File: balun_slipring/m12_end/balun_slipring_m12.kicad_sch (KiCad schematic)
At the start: 7 parts, among them J1 M12 A-8 FEMALE / EXACT MPN TBD, J2 SMA_A, J3 SMA_B, T1 ADT2-1T+, T2 ADT2-1T+

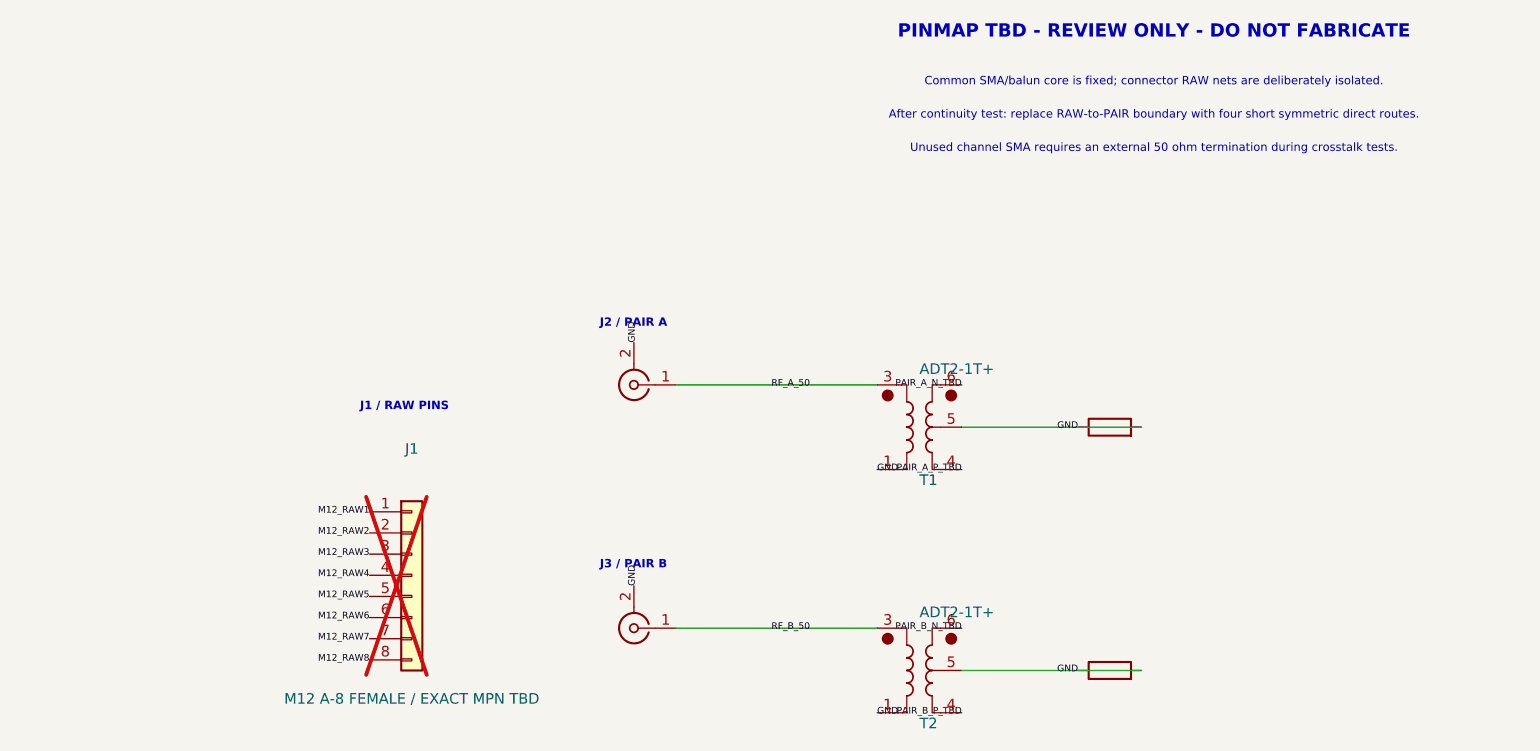
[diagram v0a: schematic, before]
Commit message: feat: finalize slip-ring fixtures and floating CT baseline
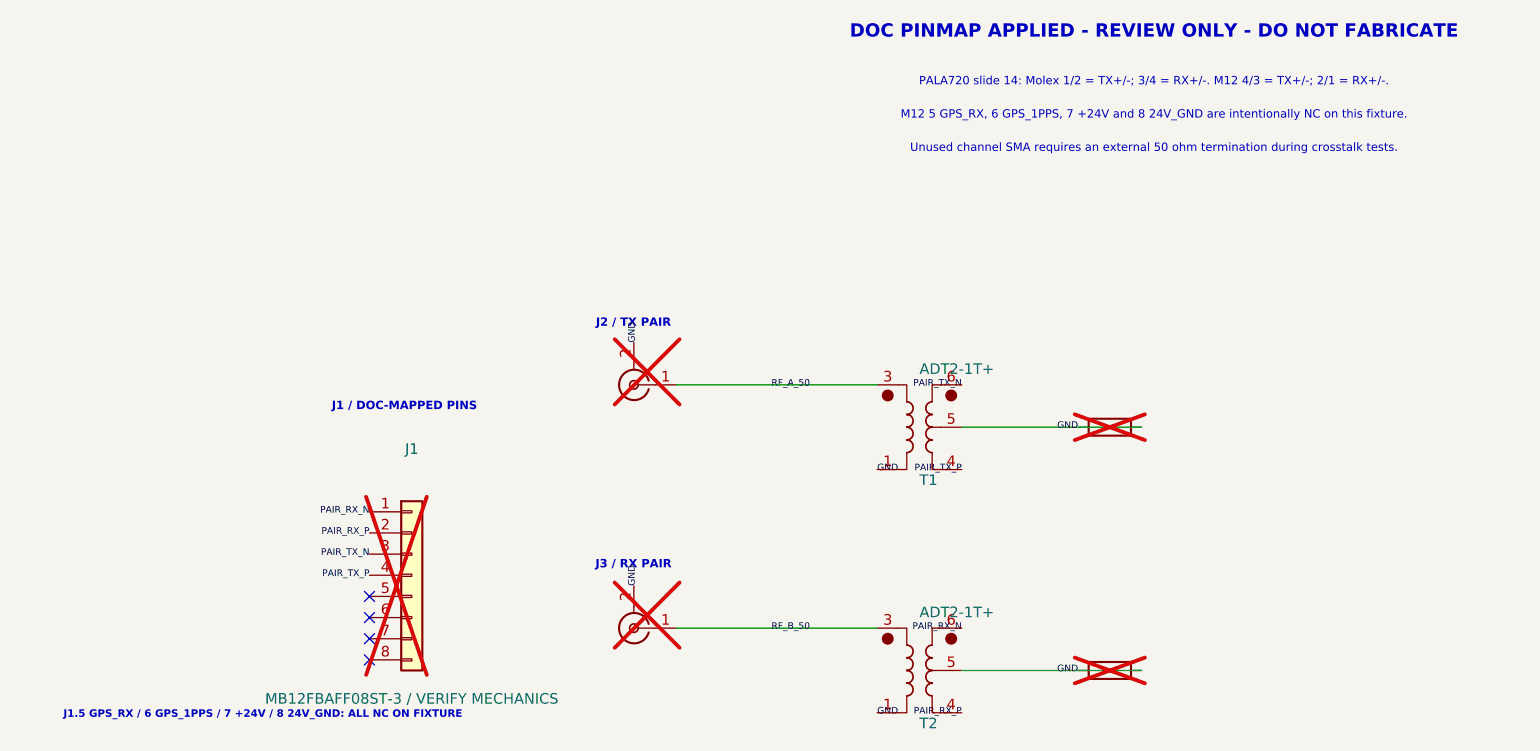
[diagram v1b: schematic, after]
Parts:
- J1: value M12 A-8 FEMALE / EXACT MPN TBD -> MB12FBAFF08ST-3 / VERIFY MECHANICS; footprint (none) -> balun_slipring_common:Finecables_MB12FBAFF08ST-3; Assembly TBD / DO NOT ORDER OR FABRICATE -> BACK-SIDE CANDIDATE; DNP UNTIL MATING, KEY/PIN-1 ORIENTATIO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; MPN Female mate for MB12MBAFF08ST-0; suffix TBD -> MB12FBAFF08ST-3 (candidate; verify mechanics); Manufacturer Finecables (candidate family) -> Finecables
- J2, J3: now not fitted
- RCT1, RCT2: Assembly FIT; remove for floating-CT comparison -> DNP; fit all four RCTs only for controlled CT-GND comparison; now not fitted
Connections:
- net PAIR_A_N_TBD is gone; now on net PAIR_TX_N: T1.6
- net PAIR_A_P_TBD is gone; now on net PAIR_TX_P: T1.4
- net PAIR_B_N_TBD is gone; now on net PAIR_RX_N: T2.6
- net PAIR_B_P_TBD is gone; now on net PAIR_RX_P: T2.4
- net M12_RAW1 renamed PAIR_RX_N
- net M12_RAW2 renamed PAIR_RX_P
- net M12_RAW3 renamed PAIR_TX_N
- net M12_RAW4 renamed PAIR_TX_P
- net M12_RAW5: no longer names the net of J1.5 (Pin_5)
- net M12_RAW6: no longer names the net of J1.6 (Pin_6)
- net M12_RAW7: no longer names the net of J1.7 (Pin_7)
- net M12_RAW8: no longer names the net of J1.8 (Pin_8)
- no-connect marks 0 -> 4
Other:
- note added: "DOC PINMAP APPLIED - REVIEW ONLY - DO NOT FABRICATE"
- note added: "J1 / DOC-MAPPED PINS"
- note added: "J1.5 GPS_RX / 6 GPS_1PPS / 7 +24V / 8 24V_GND: ALL NC ON FIXTURE"
- note added: "J2 / TX PAIR"
- note added: "J3 / RX PAIR"
- note added: "M12 5 GPS_RX, 6 GPS_1PPS, 7 +24V and 8 24V_GND are intentionally NC on this fixture."
- note added: "PALA720 slide 14: Molex 1/2 = TX+/-; 3/4 = RX+/-. M12 4/3 = TX+/-; 2/1 = RX+/-."
- note removed: "After continuity test: replace RAW-to-PAIR boundary with four short symmetric direct routes."
- note removed: "Common SMA/balun core is fixed; connector RAW nets are deliberately isolated."
- note removed: "J1 / RAW PINS"
- note removed: "J2 / PAIR A"
- note removed: "J3 / PAIR B"
- note removed: "PINMAP TBD - REVIEW ONLY - DO NOT FABRICATE"
- title: 100BASE-TX slip-ring VNA fixture - M12 END - PINMAP TBD -> 100BASE-TX slip-ring VNA fixture - M12 END - DOC PINMAP
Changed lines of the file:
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@@
 	(paper "A4")
 	(title_block
-		(title "100BASE-TX slip-ring VNA fixture - M12 END - PINMAP TBD")
+		(title "100BASE-TX slip-ring VNA fixture - M12 END - DOC PINMAP")
 		(date "2026-08-13")
-		(rev "DRAFT 0")
+		(rev "DRAFT 1")
 		(comment 1 "Two-channel 50 ohm single-ended to 100 ohm differential fixture core.")
-		(comment 2 "Connector RAW pins intentionally not mapped to balun pairs.")
-		(comment 3 "REVIEW ONLY - DO NOT FABRICATE UNTIL PINMAP AND CONNECTOR MECHANICS ARE VERIFIED.")
-	)
-	(text "PINMAP TBD - REVIEW ONLY - DO NOT FABRICATE"
+		(comment 2 "Electrical map from PALA720 slide 14; TX and RX fan-outs are connected.")
+		(comment 3 "REVIEW ONLY - DO NOT FABRICATE UNTIL CONTINUITY, CONNECTOR MECHANICS AND SMA STACK ARE VERIFIED.")
+	)
+	(text "DOC PINMAP APPLIED - REVIEW ONLY - DO NOT FABRICATE"
 		(exclude_from_sim no)
 		(at 145 25 0)
@@
 		)
 	)
-	(text "Common SMA/balun core is fixed; connector RAW nets are deliberately isolated."
+	(text "PALA720 slide 14: Molex 1/2 = TX+/-; 3/4 = RX+/-. M12 4/3 = TX+/-; 2/1 = RX+/-."
 		(exclude_from_sim no)
 		(at 145 31 0)
@@
 		)
 	)
-	(text "After continuity test: replace RAW-to-PAIR boundary with four short symmetric direct routes."
+	(text "M12 5 GPS_RX, 6 GPS_1PPS, 7 +24V and 8 24V_GND are intentionally NC on this fixture."
 		(exclude_from_sim no)
 		(at 145 35 0)
@@
 		)
 	)
-	(text "J2 / PAIR A"
+	(text "J2 / TX PAIR"
 		(exclude_from_sim no)
 		(at 82.5 60 0)
@@
 		)
 	)
-	(text "J3 / PAIR B"
+	(text "J3 / RX PAIR"
 		(exclude_from_sim no)
 		(at 82.5 89 0)
@@
 		)
 	)
-	(text "J1 / RAW PINS"
+	(text "J1 / DOC-MAPPED PINS"
 		(exclude_from_sim no)
 		(at 55 70 0)
@@
 		)
 	)
-	(label "PAIR_A_N_TBD"
+	(label "PAIR_TX_N"
 		(at 121.92 67.31 180)
 		(effects
@@
 		)
 	)
-	(label "PAIR_A_P_TBD"
+	(label "PAIR_TX_P"
 		(at 121.92 77.47 180)
 		(effects
@@
 		)
 	)
-	(label "PAIR_B_N_TBD"
+	(label "PAIR_RX_N"
 		(at 121.92 96.52 180)
 		(effects
@@
 		)
 	)
-	(label "PAIR_B_P_TBD"
+	(label "PAIR_RX_P"
 		(at 121.92 106.68 180)
 		(effects
@@
 		)
 	)
-	(label "M12_RAW1"
+	(label "PAIR_RX_N"
 		(at 50.8 82.55 180)
 		(effects
@@
 		)
 	)
-	(label "M12_RAW2"
+	(label "PAIR_RX_P"
 		(at 50.8 85.09 180)
 		(effects
@@
 		)
 	)
-	(label "M12_RAW3"
+	(label "PAIR_TX_N"
 		(at 50.8 87.63 180)
 		(effects
@@
 		)
 	)
-	(label "M12_RAW4"
+	(label "PAIR_TX_P"
 		(at 50.8 90.17 180)
 		(effects
@@
 		)
 	)
-	(label "M12_RAW5"
-		(at 50.8 92.71 180)
-		(effects
-			(font
-				(size 0.8 0.8)
-			)
-		)
-	)
-	(label "M12_RAW6"
-		(at 50.8 95.25 180)
-		(effects
-			(font
-				(size 0.8 0.8)
-			)
-		)
-	)
-	(label "M12_RAW7"
-		(at 50.8 97.79 180)
-		(effects
-			(font
-				(size 0.8 0.8)
-			)
-		)
-	)
-	(label "M12_RAW8"
-		(at 50.8 100.33 180)
-		(effects
-			(font
-				(size 0.8 0.8)
+	(no_connect
+		(at 50.8 92.71)
+	)
+	(no_connect
+		(at 50.8 95.25)
+	)
+	(no_connect
+		(at 50.8 97.79)
+	)
+	(no_connect
+		(at 50.8 100.33)
+	)
+	(text "J1.5 GPS_RX / 6 GPS_1PPS / 7 +24V / 8 24V_GND: ALL NC ON FIXTURE"
+		(exclude_from_sim no)
+		(at 38 107 0)
+		(effects
+			(font
+				(size 0.9 0.9)
+				(bold yes)
 			)
 		)
@@
 			(in_bom yes)
 			(on_board yes)
-			(in_pos_files yes)
-			(dnp no)
+			(in_pos_files no)
+			(dnp yes)
 			(property "Reference" "J2"
 				(at 82.55 67.31 0)
@@
 			(in_bom yes)
 			(on_board yes)
-			(in_pos_files yes)
-			(dnp no)
+			(in_pos_files no)
+			(dnp yes)
 			(property "Reference" "J3"
 				(at 82.55 96.52 0)
@@
 			(in_bom yes)
 			(on_board yes)
-			(in_pos_files yes)
-			(dnp no)
+			(in_pos_files no)
+			(dnp yes)
 			(property "Reference" "RCT1"
 				(at 139.7 72.39 0)
@@
 				)
 			)
-			(property "Assembly" "FIT; remove for floating-CT comparison"
+			(property "Assembly" "DNP; fit all four RCTs only for controlled CT-GND comparison"
 				(at 142.24 77.4699 0)
 				(hide yes)
@@
 			(in_bom yes)
 			(on_board yes)
-			(in_pos_files yes)
-			(dnp no)
+			(in_pos_files no)
+			(dnp yes)
 			(property "Reference" "RCT2"
 				(at 139.7 101.6 0)
@@
 				)
 			)
-			(property "Assembly" "FIT; remove for floating-CT comparison"
+			(property "Assembly" "DNP; fit all four RCTs only for controlled CT-GND comparison"
 				(at 142.24 106.6799 0)
 				(hide yes)
@@
 		(exclude_from_sim no)
 		(in_bom yes)
-		(on_board no)
+		(on_board yes)
 		(in_pos_files no)
 		(dnp yes)
@@
 			)
 		)
-		(property "Value" "M12 A-8 FEMALE / EXACT MPN TBD"
+		(property "Value" "MB12FBAFF08ST-3 / VERIFY MECHANICS"
 			(at 55.88 105 0)
 			(show_name no)
@@
 			)
 		)
-		(property "Footprint" ""
+		(property "Footprint" "balun_slipring_common:Finecables_MB12FBAFF08ST-3"
 			(at 55.88 90.17 0)
 			(hide yes)
@@
 			)
 		)
-		(property "Description" "Connector-side raw pins; intentionally isolated from balun pairs until continuity mapping is verified"
+		(property "Description" "Document-mapped M12 A-coded eight-pin female candidate; fixture uses Ethernet pins 1-4 only and intentionally leaves pins 5-8 NC"
 			(at 55.88 90.17 0)
 			(hide yes)
@@
 			)
 		)
-		(property "Manufacturer" "Finecables (candidate family)"
+		(property "Manufacturer" "Finecables"
 			(at 55.88 90.17 0)
 			(hide yes)
@@
 			)
 		)
-		(property "MPN" "Female mate for MB12MBAFF08ST-0; suffix TBD"
+		(property "MPN" "MB12FBAFF08ST-3 (candidate; verify mechanics)"
 			(at 55.88 90.17 0)
 			(hide yes)
@@
 			)
 		)
-		(property "Assembly" "TBD / DO NOT ORDER OR FABRICATE"
+		(property "Assembly" "BACK-SIDE CANDIDATE; DNP UNTIL MATING, KEY/PIN-1 ORIENTATION, PANEL SUPPORT AND AVAILABILITY ARE VERIFIED"
 			(at 55.88 90.17 0)
 			(hide yes)

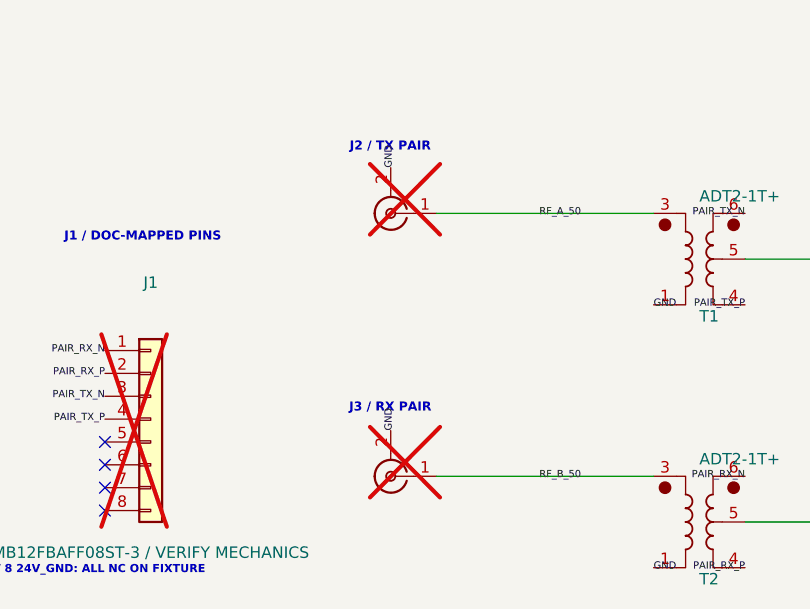
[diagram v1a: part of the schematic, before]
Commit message: feat: finalize JLC parts and measurement BOM
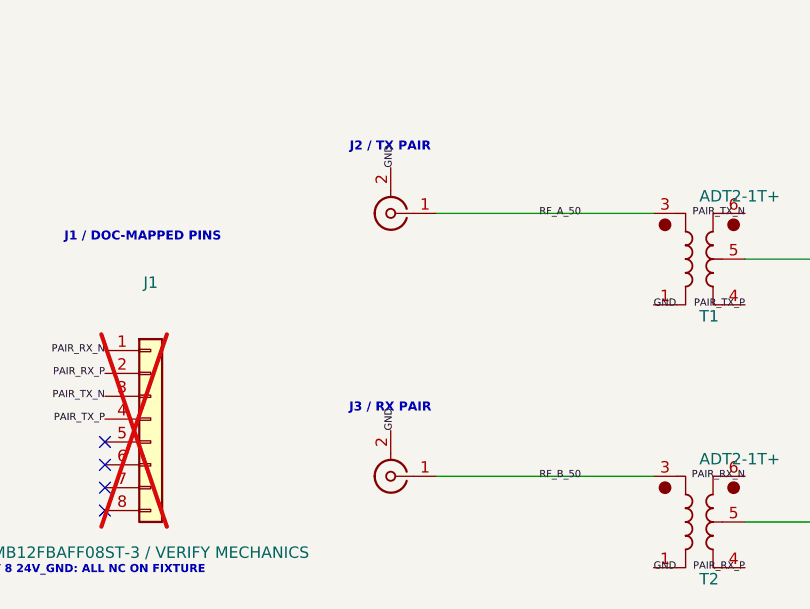
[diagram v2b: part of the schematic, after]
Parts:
- J1: LCSC Part # (none) -> C22378785
- J2, J3: footprint Connector_Coaxial:SMA_Amphenol_132289_EdgeMount -> balun_slipring_common:SMA_MyAntenna_A-SMA-KE-16.5A_EdgeMount; Assembly DNP UNTIL STACK/CONNECTOR DECISION -> FIT; JLC C22467617; Standard PCBA / wave-solder review; LCSC Part # (none) -> C22467617; MPN 132289 -> A-SMA-KE-16.5A; Manufacturer Amphenol RF -> MyAntenna; now fitted
- RCT1, RCT2: LCSC Part # (none) -> C17477
- T1, T2: LCSC Part # (none) -> C5223988
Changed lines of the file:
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@@
 		(comment 1 "Two-channel 50 ohm single-ended to 100 ohm differential fixture core.")
 		(comment 2 "Electrical map from PALA720 slide 14; TX and RX fan-outs are connected.")
-		(comment 3 "REVIEW ONLY - DO NOT FABRICATE UNTIL CONTINUITY, CONNECTOR MECHANICS AND SMA STACK ARE VERIFIED.")
+		(comment 3 "REVIEW ONLY - DO NOT FABRICATE UNTIL CONTINUITY AND ENDPOINT CONNECTOR MECHANICS ARE VERIFIED.")
 	)
 	(text "DOC PINMAP APPLIED - REVIEW ONLY - DO NOT FABRICATE"
@@
 			(in_bom yes)
 			(on_board yes)
-			(in_pos_files no)
-			(dnp yes)
+			(in_pos_files yes)
+			(dnp no)
 			(property "Reference" "J2"
 				(at 82.55 67.31 0)
@@
 				)
 			)
-			(property "Footprint" "Connector_Coaxial:SMA_Amphenol_132289_EdgeMount"
+			(property "Footprint" "balun_slipring_common:SMA_MyAntenna_A-SMA-KE-16.5A_EdgeMount"
 				(at 82.55 67.31 0)
 				(hide yes)
@@
 				)
 			)
-			(property "Datasheet" "https://www.amphenolrf.com/132289.html"
+			(property "Datasheet" "https://datasheet.lcsc.com/datasheet/pdf/92633ab2cf30de4413e1a152c04a3ed5.pdf?productCode=C22467617"
 				(at 82.55 67.31 0)
 				(hide yes)
@@
 				)
 			)
-			(property "Manufacturer" "Amphenol RF"
+			(property "Manufacturer" "MyAntenna"
 				(at 85.09 72.3899 0)
 				(hide yes)
@@
 				)
 			)
-			(property "MPN" "132289"
+			(property "MPN" "A-SMA-KE-16.5A"
 				(at 85.09 72.3899 0)
 				(hide yes)
@@
 				)
 			)
-			(property "Assembly" "DNP UNTIL STACK/CONNECTOR DECISION"
+			(property "Assembly" "FIT; JLC C22467617; Standard PCBA / wave-solder review"
 				(at 85.09 72.3899 0)
 				(hide yes)
@@
 					)
 				)
+			)
+			(property "LCSC Part #" "C22467617"
+				(at 0 0 0)
+				(hide yes)
+				(show_name no)
+				(do_not_autoplace no)
+				(effects (font (size 1.27 1.27)))
 			)
 			(pin "1"
@@
 			(in_bom yes)
 			(on_board yes)
-			(in_pos_files no)
-			(dnp yes)
+			(in_pos_files yes)
+			(dnp no)
 			(property "Reference" "J3"
 				(at 82.55 96.52 0)
@@
 				)
 			)
-			(property "Footprint" "Connector_Coaxial:SMA_Amphenol_132289_EdgeMount"
+			(property "Footprint" "balun_slipring_common:SMA_MyAntenna_A-SMA-KE-16.5A_EdgeMount"
 				(at 82.55 96.52 0)
 				(hide yes)
@@
 				)
 			)
-			(property "Datasheet" "https://www.amphenolrf.com/132289.html"
+			(property "Datasheet" "https://datasheet.lcsc.com/datasheet/pdf/92633ab2cf30de4413e1a152c04a3ed5.pdf?productCode=C22467617"
 				(at 82.55 96.52 0)
 				(hide yes)
@@
 				)
 			)
-			(property "Manufacturer" "Amphenol RF"
+			(property "Manufacturer" "MyAntenna"
 				(at 85.09 101.5999 0)
 				(hide yes)
@@
 				)
 			)
-			(property "MPN" "132289"
+			(property "MPN" "A-SMA-KE-16.5A"
 				(at 85.09 101.5999 0)
 				(hide yes)
@@
 				)
 			)
-			(property "Assembly" "DNP UNTIL STACK/CONNECTOR DECISION"
+			(property "Assembly" "FIT; JLC C22467617; Standard PCBA / wave-solder review"
 				(at 85.09 101.5999 0)
 				(hide yes)
@@
 					)
 				)
+			)
+			(property "LCSC Part #" "C22467617"
+				(at 0 0 0)
+				(hide yes)
+				(show_name no)
+				(do_not_autoplace no)
+				(effects (font (size 1.27 1.27)))
 			)
 			(pin "1"
@@
 				)
 			)
+			(property "LCSC Part #" "C5223988"
+				(at 119.38 77.4699 0)
+				(hide yes)
+				(show_name no)
+				(do_not_autoplace no)
+				(effects
+					(font
+						(size 1.27 1.27)
+					)
+				)
+			)
 			(pin "1"
 			)
@@
 				)
 			)
+			(property "LCSC Part #" "C5223988"
+				(at 119.38 106.6799 0)
+				(hide yes)
+				(show_name no)
+				(do_not_autoplace no)
+				(effects
+					(font
+						(size 1.27 1.27)
+					)
+				)
+			)
 			(pin "1"
 			)
@@
 				)
 			)
+			(property "LCSC Part #" "C17477"
+				(at 142.24 77.4699 0)
+				(hide yes)
+				(show_name no)
+				(do_not_autoplace no)
+				(effects
+					(font
+						(size 1.27 1.27)
+					)
+				)
+			)
 			(pin "1"
 			)
@@
 			)
 			(property "Assembly" "DNP; fit all four RCTs only for controlled CT-GND comparison"
+				(at 142.24 106.6799 0)
+				(hide yes)
+				(show_name no)
+				(do_not_autoplace no)
+				(effects
+					(font
+						(size 1.27 1.27)
+					)
+				)
+			)
+			(property "LCSC Part #" "C17477"
 				(at 142.24 106.6799 0)
 				(hide yes)
@@
 			(at 55.88 90.17 0)
 			(hide yes)
+			(show_name no)
+			(do_not_autoplace no)
+			(effects
+				(font
+					(size 1.27 1.27)
+				)
+			)
+		)
+		(property "LCSC Part #" "C22378785"
+			(at 55.88 90.17 0)
+			(hide yes)

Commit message: feat: add complete VNA fixture design set
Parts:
- J1: Assembly BACK-SIDE CANDIDATE; DNP UNTIL MATING, KEY/PIN-1 ORIENTATIO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 -> PCB B-SIDE ELECTRICAL CANDIDATE; DNP UNTIL MATING, KEY/PIN-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
- RCT1, RCT2: MPN 0 ohm 0805 -> 0805W8F0000T5E; Manufacturer ANY -> UNI-ROYAL
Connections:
- net GND: no longer RCT1.2, RCT2.2, T1.5, T2.5
- new net: RCT1.2, T1.5
- new net: RCT2.2, T2.5
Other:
- note added: "+24V / NC"
- note added: "1"
- note added: "1. REVIEW ONLY - DO NOT FABRICATE. Connector fit / mechanics remain on HOLD."
- note added: "1:2 impedance"
- note added: "1PPS / NC"
- note added: "2"
- note added: "2. Existing J1 DNP is retained as a candidate HOLD; not a connectorless order."
- note added: "24V RTN / NC"
- note added: "3"
- note added: "3. RCT1/RCT2 DNP: CT-FLOAT baseline. No on-board 100 ohm load."
- note added: "4"
- note added: "4. M12 pins 5/6/7/8 are NC; disconnect power and all active equipment."
- note added: "5. Two-board tests: terminate the two unused SMA ports with 50 ohm loads."
- note added: "6. Coax O/S/L + THRU does not remove the balun / PCB / connector response."
- note added: "A / TX PAIR - 50 ohm SMA to 100 ohm differential"
- note added: "ASSEMBLY / MEASUREMENT NOTES"
- note added: "B / RX PAIR - 50 ohm SMA to 100 ohm differential"
- note added: "DNP / CT FLOAT"
- note added: "FEMALE PCB mate / candidate on HOLD"
- note added: "GPS RX / NC"
- note added: "Logical pin numbers; verify mating-face / PCB view."
- note added: "M12"
- note added: "M12 END / J1"
- note added: "MOLEX"
- note added: "NOT interchangeable with the LLC / actuator M12 fixture."
- note added: "RX+"
- note added: "RX-"
- note added: "SIGNAL"
- note added: "SLIPRING / M12 END"
- note added: "SLIPRING MAP / PALA720 SLIDE 14"
- note added: "TX+"
- note added: "TX-"
- note added: "슬립링 측정 지그 | M12 END"
- note removed: "DOC PINMAP APPLIED - REVIEW ONLY - DO NOT FABRICATE"
- note removed: "J1 / DOC-MAPPED PINS"
- note removed: "J1.5 GPS_RX / 6 GPS_1PPS / 7 +24V / 8 24V_GND: ALL NC ON FIXTURE"
- note removed: "J2 / TX PAIR"
- note removed: "J3 / RX PAIR"
- note removed: "M12 5 GPS_RX, 6 GPS_1PPS, 7 +24V and 8 24V_GND are intentionally NC on this fixture."
- note removed: "PALA720 slide 14: Molex 1/2 = TX+/-; 3/4 = RX+/-. M12 4/3 = TX+/-; 2/1 = RX+/-."
- note removed: "Unused channel SMA requires an external 50 ohm termination during crosstalk tests."
- title: 100BASE-TX slip-ring VNA fixture - M12 END - DOC PINMAP -> SLIPRING / M12 END
- moved on the sheet: J1, T1, T2
